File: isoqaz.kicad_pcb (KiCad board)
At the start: 2 copper layers, 21 parts, among them J1 USB_C_Receptacle_USB2.0, U1 STM32F072CBT6, U2 PRTR5V0U2X, U3 XC6206PxxxMR-Regulator_Linear

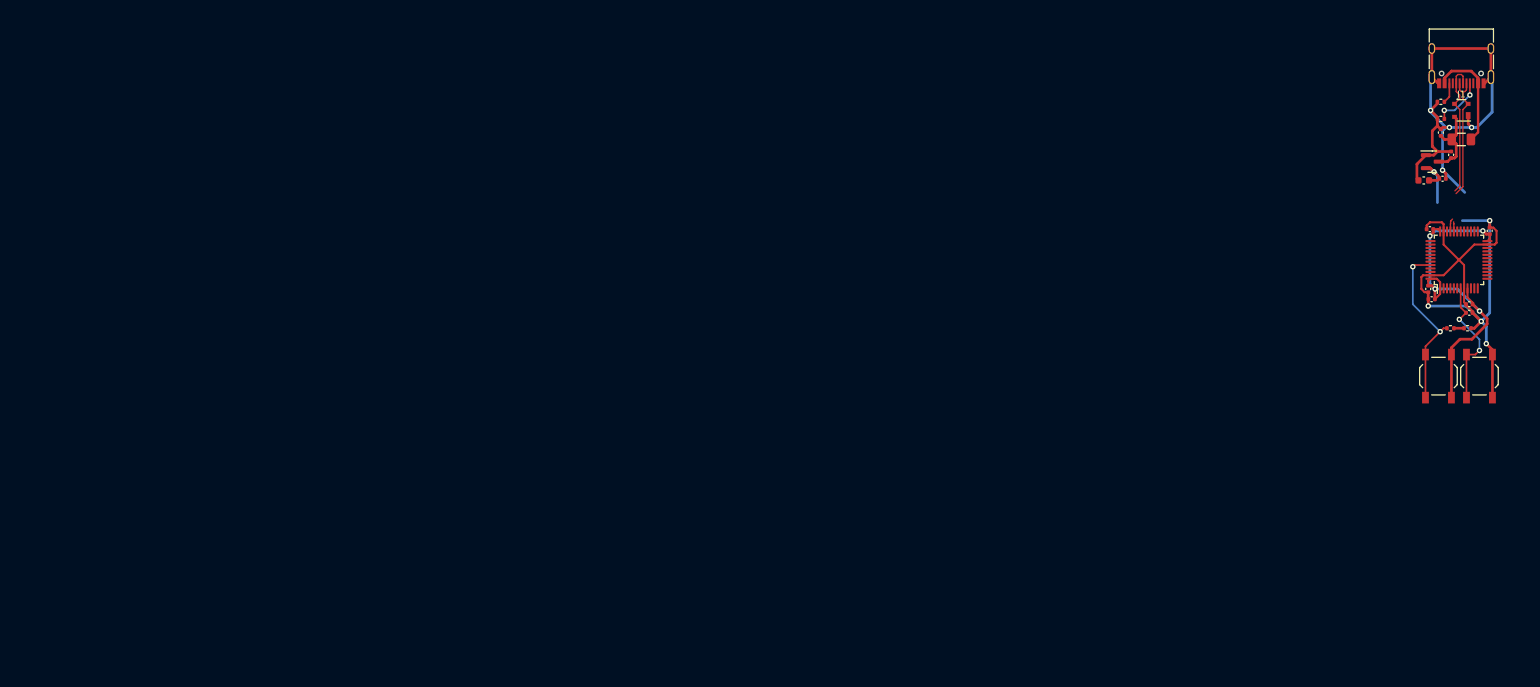
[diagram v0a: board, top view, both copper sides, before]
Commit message: added case files, finished pcb
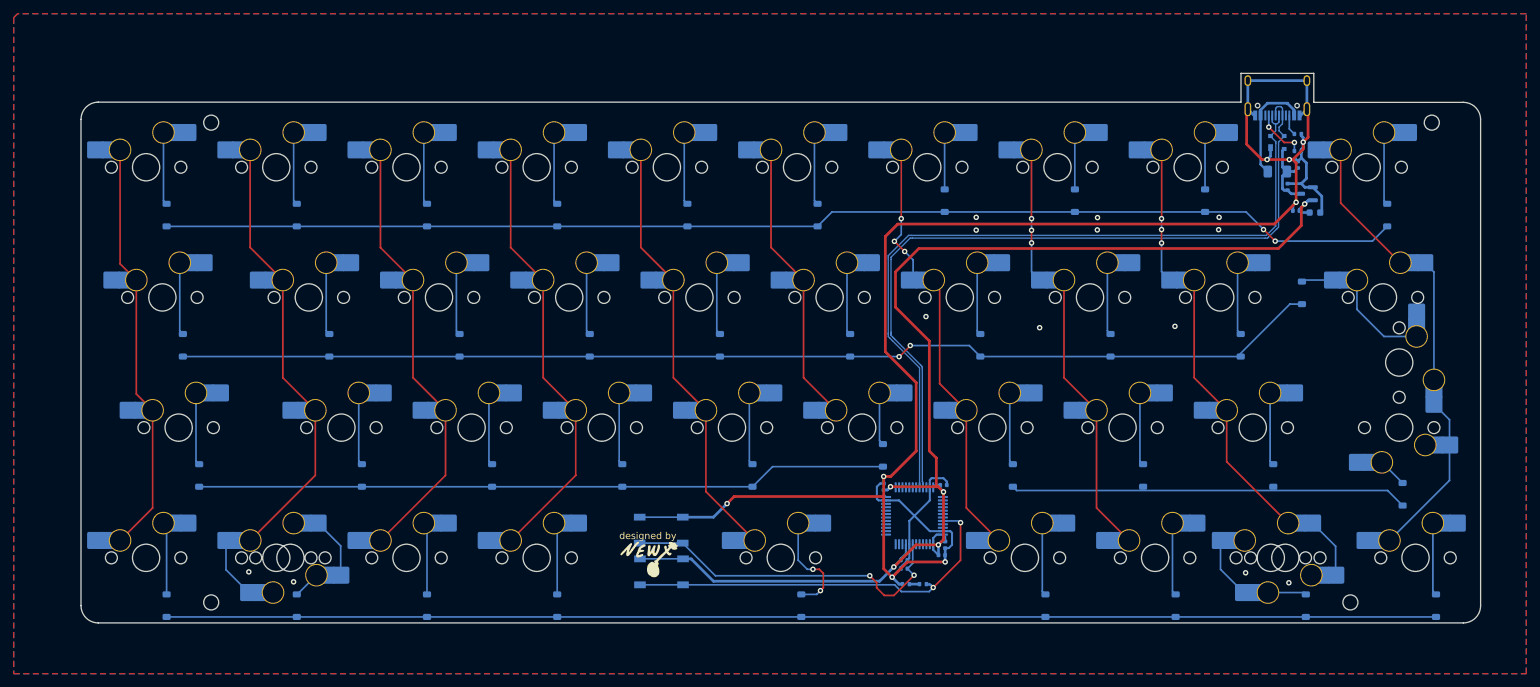
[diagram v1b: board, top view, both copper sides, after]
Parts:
- added D1: D_Small, Diode_SMD:D_SOD-123, B.Cu at (58.9, 69.3)
- added D10: D_Small, Diode_SMD:D_SOD-123, B.Cu at (237.5, 69.3)
- added D11: D_Small, Diode_SMD:D_SOD-123, B.Cu at (61.3, 88.4)
- added D12: D_Small, Diode_SMD:D_SOD-123, B.Cu at (82.7, 88.4)
- added D13: D_Small, Diode_SMD:D_SOD-123, B.Cu at (101.8, 88.4)
- added D14: D_Small, Diode_SMD:D_SOD-123, B.Cu at (120.8, 88.4)
- added D15: D_Small, Diode_SMD:D_SOD-123, B.Cu at (139.9, 88.4)
- added D16: D_Small, Diode_SMD:D_SOD-123, B.Cu at (158.9, 88.4)
- added D17: D_Small, Diode_SMD:D_SOD-123, B.Cu at (178.0, 88.4)
- added D18: D_Small, Diode_SMD:D_SOD-123, B.Cu at (197.0, 88.4)
- added D19: D_Small, Diode_SMD:D_SOD-123, B.Cu at (216.1, 88.4)
- added D2: D_Small, Diode_SMD:D_SOD-123, B.Cu at (78.0, 69.3)
- added D20: D_Small, Diode_SMD:D_SOD-123, B.Cu at (225.1, 80.7)
- added D21: D_Small, Diode_SMD:D_SOD-123, B.Cu at (63.7, 107.4)
- added D22: D_Small, Diode_SMD:D_SOD-123, B.Cu at (87.5, 107.4)
- added D23: D_Small, Diode_SMD:D_SOD-123, B.Cu at (106.6, 107.4)
- added D24: D_Small, Diode_SMD:D_SOD-123, B.Cu at (125.6, 107.4)
- added D25: D_Small, Diode_SMD:D_SOD-123, B.Cu at (144.7, 107.4)
- added D26: D_Small, Diode_SMD:D_SOD-123, B.Cu at (163.8, 104.5)
- added D27: D_Small, Diode_SMD:D_SOD-123, B.Cu at (182.8, 107.4)
- added D28: D_Small, Diode_SMD:D_SOD-123, B.Cu at (201.8, 107.4)
- added D29: D_Small, Diode_SMD:D_SOD-123, B.Cu at (220.9, 107.4)
- added D3: D_Small, Diode_SMD:D_SOD-123, B.Cu at (97.0, 69.3)
- added D30: D_Small, Diode_SMD:D_SOD-123, B.Cu at (239.8, 110.2)
- added D31: D_Small, Diode_SMD:D_SOD-123, B.Cu at (58.9, 126.5)
- added D32: D_Small, Diode_SMD:D_SOD-123, B.Cu at (78.0, 126.5)
- added D33: D_Small, Diode_SMD:D_SOD-123, B.Cu at (97.0, 126.5)
- added D34: D_Small, Diode_SMD:D_SOD-123, B.Cu at (116.1, 126.5)
- added D35: D_Small, Diode_SMD:D_SOD-123, B.Cu at (151.8, 126.5)
- added D36: D_Small, Diode_SMD:D_SOD-123, B.Cu at (187.5, 126.5)
- added D37: D_Small, Diode_SMD:D_SOD-123, B.Cu at (206.6, 126.5)
- added D38: D_Small, Diode_SMD:D_SOD-123, B.Cu at (225.6, 126.5)
- added D39: D_Small, Diode_SMD:D_SOD-123, B.Cu at (244.7, 126.5)
- added D4: D_Small, Diode_SMD:D_SOD-123, B.Cu at (116.1, 69.3)
- added D5: D_Small, Diode_SMD:D_SOD-123, B.Cu at (135.1, 69.3)
- added D6: D_Small, Diode_SMD:D_SOD-123, B.Cu at (154.2, 69.3)
- added D7: D_Small, Diode_SMD:D_SOD-123, B.Cu at (172.8, 67.2)
- added D8: D_Small, Diode_SMD:D_SOD-123, B.Cu at (191.8, 67.2)
- added D9: D_Small, Diode_SMD:D_SOD-123, B.Cu at (210.9, 67.2)
- added MX1: MX_SW_HS, marbastlib-mx:SW_MX_HS_CPG151101S11_1u, B.Cu at (55.9, 62.3)
- added MX10: MX_SW_HS, marbastlib-mx:SW_MX_HS_CPG151101S11_1u, B.Cu at (234.5, 62.3)
- added MX11: MX_SW_HS, marbastlib-mx:SW_MX_HS_CPG151101S11_1u, B.Cu at (58.3, 81.4)
- added MX12: MX_SW_HS, marbastlib-mx:SW_MX_HS_CPG151101S11_1u, B.Cu at (79.8, 81.4)
- added MX13: MX_SW_HS, marbastlib-mx:SW_MX_HS_CPG151101S11_1u, B.Cu at (98.8, 81.4)
- added MX14: MX_SW_HS, marbastlib-mx:SW_MX_HS_CPG151101S11_1u, B.Cu at (117.8, 81.4)
- added MX15: MX_SW_HS, marbastlib-mx:SW_MX_HS_CPG151101S11_1u, B.Cu at (136.9, 81.4)
- added MX16: MX_SW_HS, marbastlib-mx:SW_MX_HS_CPG151101S11_1u, B.Cu at (155.9, 81.4)
- added MX17: MX_SW_HS, marbastlib-mx:SW_MX_HS_CPG151101S11_1u, B.Cu at (175.0, 81.4)
- added MX18: MX_SW_HS, marbastlib-mx:SW_MX_HS_CPG151101S11_1u, B.Cu at (194.1, 81.4)
- added MX19: MX_SW_HS, marbastlib-mx:SW_MX_HS_CPG151101S11_1u, B.Cu at (213.1, 81.4)
- added MX2: MX_SW_HS, marbastlib-mx:SW_MX_HS_CPG151101S11_1u, B.Cu at (75.0, 62.3)
- added MX20: MX_SW_HS, marbastlib-mx:SW_MX_HS_CPG151101S11_1u, B.Cu at (236.9, 81.4)
- added MX21: MX_SW_HS, marbastlib-mx:SW_MX_HS_CPG151101S11_1u, B.Cu at (60.7, 100.4)
- added MX22: MX_SW_HS, marbastlib-mx:SW_MX_HS_CPG151101S11_1u, B.Cu at (84.5, 100.4)
- added MX23: MX_SW_HS, marbastlib-mx:SW_MX_HS_CPG151101S11_1u, B.Cu at (103.6, 100.4)
- added MX24: MX_SW_HS, marbastlib-mx:SW_MX_HS_CPG151101S11_1u, B.Cu at (122.6, 100.4)
- added MX25: MX_SW_HS, marbastlib-mx:SW_MX_HS_CPG151101S11_1u, B.Cu at (141.7, 100.4)
- added MX26: MX_SW_HS, marbastlib-mx:SW_MX_HS_CPG151101S11_1u, B.Cu at (160.7, 100.4)
- added MX27: MX_SW_HS, marbastlib-mx:SW_MX_HS_CPG151101S11_1u, B.Cu at (179.8, 100.4)
- added MX28: MX_SW_HS, marbastlib-mx:SW_MX_HS_CPG151101S11_1u, B.Cu at (198.8, 100.4)
- added MX29: MX_SW_HS, marbastlib-mx:SW_MX_HS_CPG151101S11_1u, B.Cu at (217.9, 100.4)
- added MX3: MX_SW_HS, marbastlib-mx:SW_MX_HS_CPG151101S11_1u, B.Cu at (94.0, 62.3)
- added MX30: MX_SW_HS, marbastlib-mx:SW_MX_HS_CPG151101S11_1u, B.Cu at (239.3, 100.4)
- added MX31: MX_SW_HS, marbastlib-mx:SW_MX_HS_CPG151101S11_1u, B.Cu at (55.9, 119.5)
- added MX32: MX_SW_HS, marbastlib-mx:SW_MX_HS_CPG151101S11_1u, B.Cu at (75.0, 119.5)
- added MX33: MX_SW_HS, marbastlib-mx:SW_MX_HS_CPG151101S11_1u, B.Cu at (94.0, 119.5)
- added MX34: MX_SW_HS, marbastlib-mx:SW_MX_HS_CPG151101S11_1u, B.Cu at (113.1, 119.5)
- added MX35: MX_SW_HS, marbastlib-mx:SW_MX_HS_CPG151101S11_1u, B.Cu at (148.8, 119.5)
- added MX36: MX_SW_HS, marbastlib-mx:SW_MX_HS_CPG151101S11_1u, B.Cu at (184.5, 119.5)
- added MX37: MX_SW_HS, marbastlib-mx:SW_MX_HS_CPG151101S11_1u, B.Cu at (203.6, 119.5)
- added MX38: MX_SW_HS, marbastlib-mx:SW_MX_HS_CPG151101S11_1u, B.Cu at (222.6, 119.5)
- added MX39: MX_SW_HS, marbastlib-mx:SW_MX_HS_CPG151101S11_1u, B.Cu at (241.7, 119.5)
- added MX4: MX_SW_HS, marbastlib-mx:SW_MX_HS_CPG151101S11_1u, B.Cu at (113.1, 62.3)
- added MX40: MX_SW_HS, marbastlib-mx:SW_MX_HS_CPG151101S11_1u, B.Cu at (77.1, 119.5)
- added MX41: MX_SW_HS, marbastlib-mx:SW_MX_HS_CPG151101S11_1u, B.Cu at (220.5, 119.5)
- added MX42: MX_SW_HS, marbastlib-mx:SW_MX_HS_CPG151101S11_1u, B.Cu at (239.3, 90.9)
- added MX5: MX_SW_HS, marbastlib-mx:SW_MX_HS_CPG151101S11_1u, B.Cu at (132.1, 62.3)
- added MX6: MX_SW_HS, marbastlib-mx:SW_MX_HS_CPG151101S11_1u, B.Cu at (151.2, 62.3)
- added MX7: MX_SW_HS, marbastlib-mx:SW_MX_HS_CPG151101S11_1u, B.Cu at (170.2, 62.3)
- added MX8: MX_SW_HS, marbastlib-mx:SW_MX_HS_CPG151101S11_1u, B.Cu at (189.3, 62.3)
- added MX9: MX_SW_HS, marbastlib-mx:SW_MX_HS_CPG151101S11_1u, B.Cu at (208.3, 62.3)
- added REF**: MountingHole_2.2mm_M2, MountingHole:MountingHole_2.2mm_M2, F.Cu at (65.5, 126.0)
- added REF**: MountingHole_2.2mm_M2, MountingHole:MountingHole_2.2mm_M2, F.Cu at (65.5, 55.8)
- added REF**: MountingHole_2.2mm_M2, MountingHole:MountingHole_2.2mm_M2, F.Cu at (244.1, 55.8)
- added REF**: MountingHole_2.2mm_M2, MountingHole:MountingHole_2.2mm_M2, F.Cu at (232.2, 126.0)
- BOOT1, C1, C10, C2, C3, C4, C5, C6, C7, C8, C9, F1, J1, R1, R2, R3, R4, RST1, U1, U2, U3: moved to B.Cu
- moved RST1 121.8 mm to (131.3, 115.4), turned to 0 degrees
- moved BOOT1 117.2 mm to (131.3, 121.5), turned to 180 degrees
- moved C4 96.3 mm to (163.9, 109.1)
- moved C1 90.8 mm to (166.8, 121.1), turned to 180 degrees
- moved C7 90.8 mm to (166.8, 119.8), turned to 0 degrees
- moved R4 90.3 mm to (167.1, 123.3), turned to 180 degrees
- moved U1 88.0 mm to (168.4, 113.3)
- moved R3 85.8 mm to (169.6, 123.3), turned to 180 degrees
- moved C6 80.9 mm to (172.4, 119.1), turned to 0 degrees
- moved C3 80.4 mm to (172.6, 108.8), turned to 0 degrees
- moved C5 80.0 mm to (172.9, 117.6)
- moved F1 27.3 mm to (221.5, 63.0), turned to 0 degrees
- moved J1 27.3 mm to (221.5, 50.7), turned to 0 degrees
- moved U2 27.3 mm to (221.5, 58.7), turned to 0 degrees
- moved C9 24.4 mm to (223.0, 65.2)
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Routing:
- net ROW4: track 0.00 -> 185.7 mm
- net ROW0: track 0.00 -> 182.1 mm, vias 0 -> 2
- net ROW1: track 0.00 -> 168.3 mm, vias 0 -> 2
- net +3V3: track 66.8 -> 184.6 mm
- net GND: track 157.3 -> 275.0 mm, vias 8 -> 21
- net ROW2: track 0.00 -> 101.3 mm
- net D+: track 22.1 -> 114.6 mm
- net D-: track 20.5 -> 113.0 mm
- net COL1: track 0.00 -> 74.1 mm
- net COL8: track 0.00 -> 69.8 mm, vias 0 -> 3
- net COL3: track 0.00 -> 65.0 mm
- net COL2: track 0.00 -> 65.0 mm
- net COL4: track 0.00 -> 64.1 mm
- net COL6: track 0.00 -> 62.9 mm, vias 0 -> 3
- net COL9: track 0.00 -> 62.4 mm
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- added copper zone on B.Cu, net GND
- added copper zone on F.Cu, net GND
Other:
- board outline added: 204.8 x 80.4 mm
- board text added: "designed by"
